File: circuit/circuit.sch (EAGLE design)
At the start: 60 parts, among them IC1 74HC04N, X1 PSS 254/8G

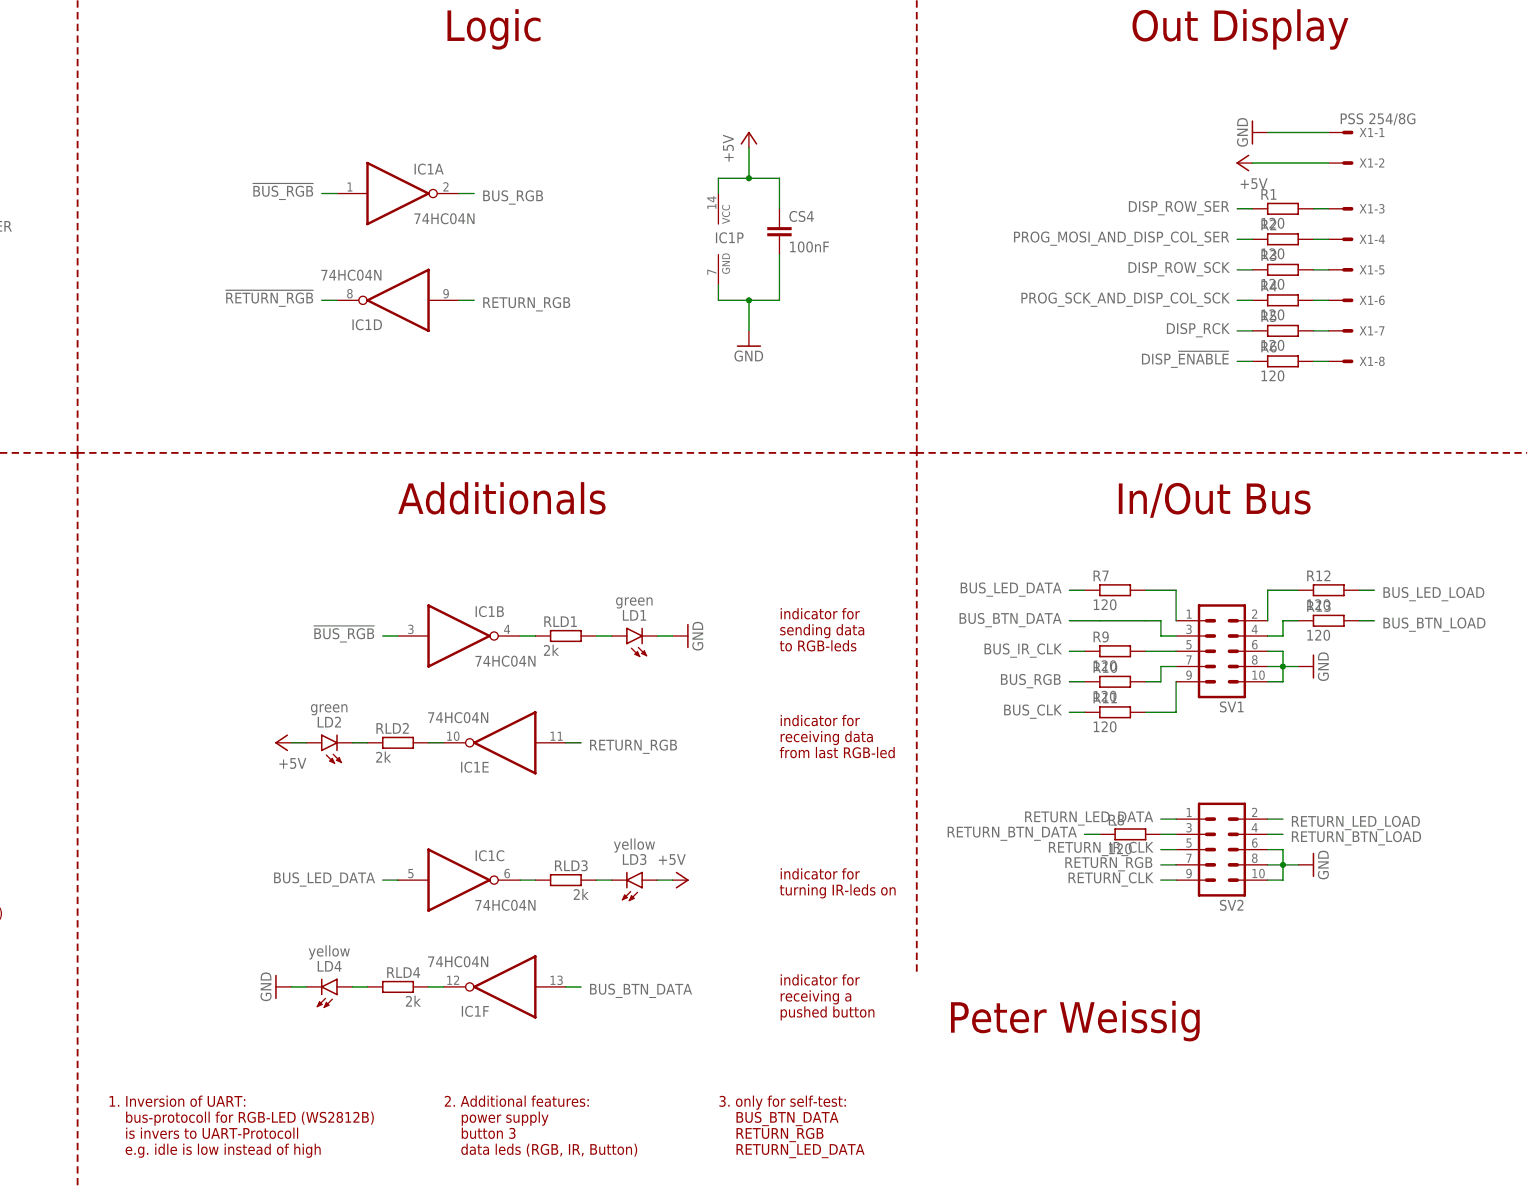
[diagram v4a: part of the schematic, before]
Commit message: updated circuit   + changed font type and size (e.g. fixed size of url)   + updated cooling pad for voltage regulator   + added more spacing at buttons (between pinheads and resistors)   + updated part-list
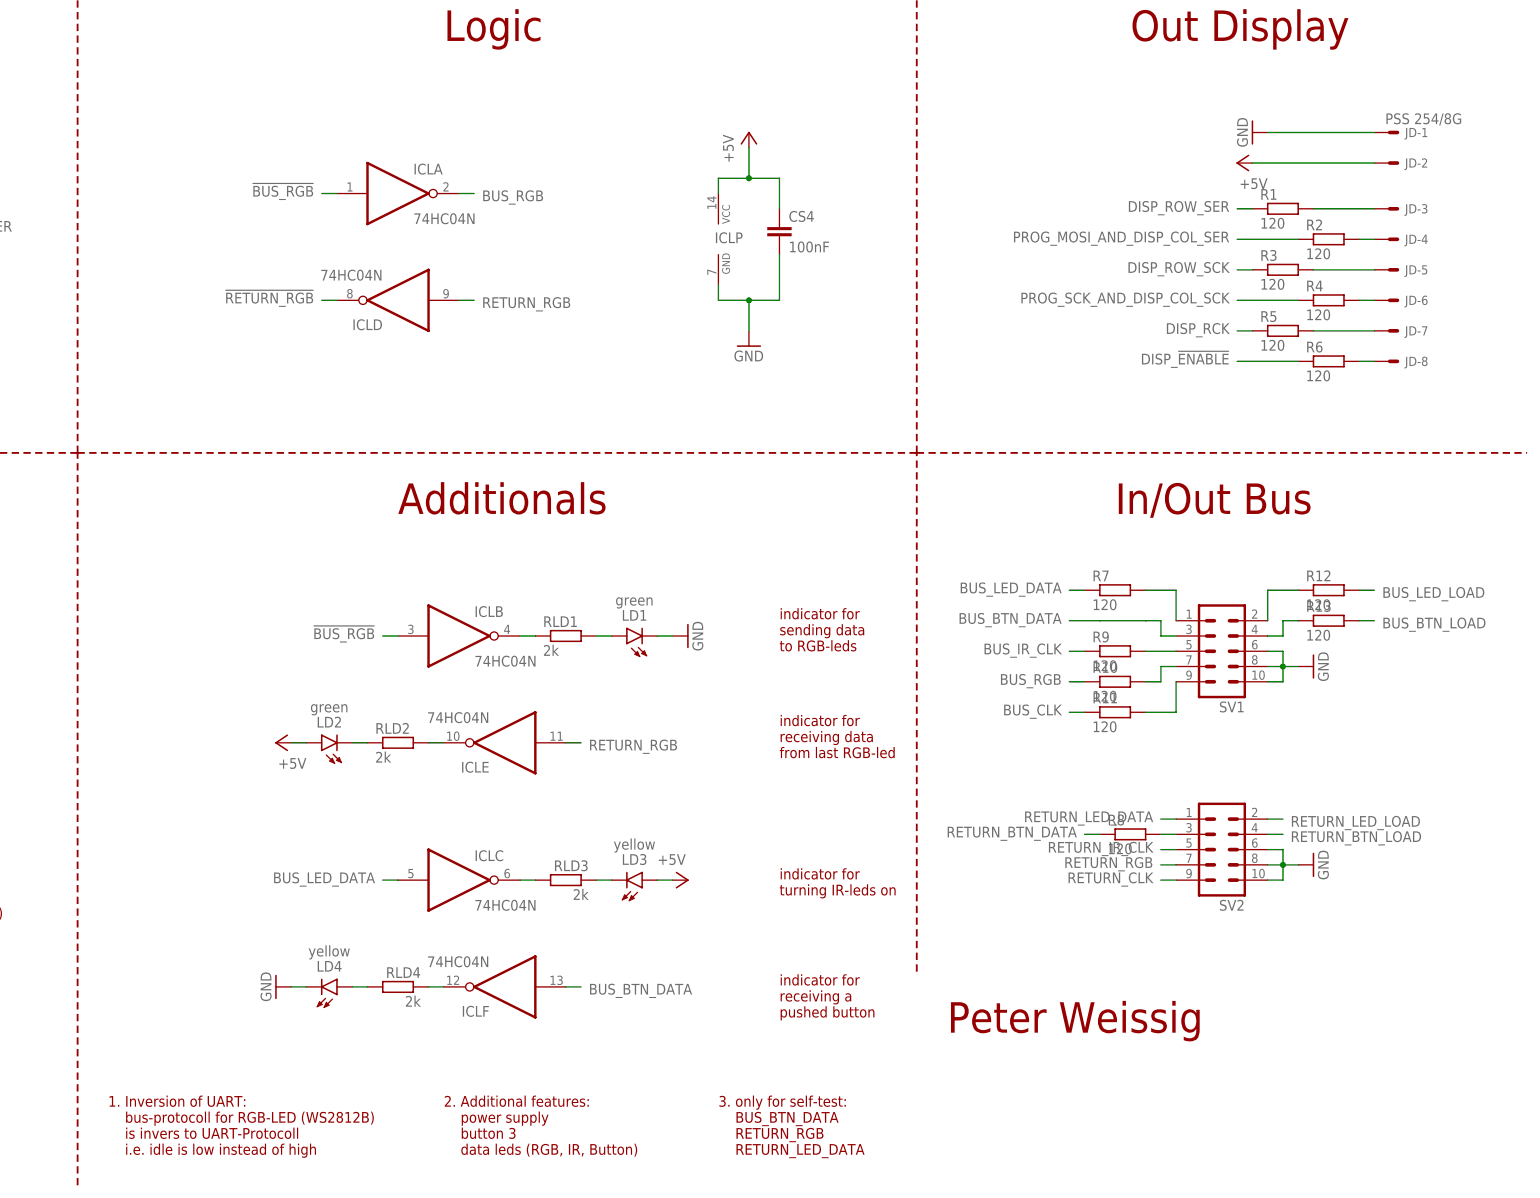
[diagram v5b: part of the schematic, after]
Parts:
- removed X1: PSS 254/8G, con-molex:22-23-2081
- added JD: PSS 254/8G, con-molex:22-23-2081
- renumbered IC1 to ICL
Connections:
- net +5V: now also JD-2.S; no longer X1-2.S
- net GND: now also JD-1.S; no longer X1-1.S
- net N$20: now also JD-3.S; no longer X1-3.S
- net N$21: now also JD-4.S; no longer X1-4.S
- net N$22: now also JD-5.S; no longer X1-5.S
- net N$23: now also JD-6.S; no longer X1-6.S
- net N$24: now also JD-7.S; no longer X1-7.S
- net N$25: now also JD-8.S; no longer X1-8.S
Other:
- note added: "1. Inversion of UART: bus-protocoll for RGB-LED (WS2812B) is invers to UART-Protocoll i.e. idle is low instead of high"
- note removed: "1. Inversion of UART: bus-protocoll for RGB-LED (WS2812B) is invers to UART-Protocoll e.g. idle is low instead of high"
- moved on the sheet: R2, R4, R6

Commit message: minor fixes:   + updated crystal from 16 to 20 MHz   + updated package for SMD resistors (1206 instead of 0805)   + fixed wrong caption (from 2019 to 2020) ==> newly exported images and elecrow files ==> updated part list and reichelt shopping cart
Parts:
- R1, R10, R11, R12, R13, R2, R3, R4, R5, R6, R7, R8, R9: device rcl:R-EU_R0805 -> rcl:R-EU_R1206W
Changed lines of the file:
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@@
 <grid distance="0.1" unitdist="inch" unit="inch" style="lines" multiple="1" display="no" altdistance="0.01" altunitdist="inch" altunit="inch"/>
 <layers>
-<layer number="1" name="Top" color="4" fill="1" visible="no" active="no"/>
-<layer number="16" name="Bottom" color="1" fill="1" visible="no" active="no"/>
-<layer number="17" name="Pads" color="2" fill="1" visible="no" active="no"/>
-<layer number="18" name="Vias" color="2" fill="1" visible="no" active="no"/>
-<layer number="19" name="Unrouted" color="6" fill="1" visible="no" active="no"/>
-<layer number="20" name="Dimension" color="15" fill="1" visible="no" active="no"/>
-<layer number="21" name="tPlace" color="7" fill="1" visible="no" active="no"/>
-<layer number="22" name="bPlace" color="7" fill="1" visible="no" active="no"/>
-<layer number="23" name="tOrigins" color="15" fill="1" visible="no" active="no"/>
-<layer number="24" name="bOrigins" color="15" fill="1" visible="no" active="no"/>
-<layer number="25" name="tNames" color="7" fill="1" visible="no" active="no"/>
-<layer number="26" name="bNames" color="7" fill="1" visible="no" active="no"/>
-<layer number="27" name="tValues" color="7" fill="1" visible="no" active="no"/>
-<layer number="28" name="bValues" color="7" fill="1" visible="no" active="no"/>
+<layer number="1" name="Top" color="4" fill="1" visible="yes" active="no"/>
+<layer number="16" name="Bottom" color="1" fill="1" visible="yes" active="no"/>
+<layer number="17" name="Pads" color="2" fill="1" visible="yes" active="no"/>
+<layer number="18" name="Vias" color="2" fill="1" visible="yes" active="no"/>
+<layer number="19" name="Unrouted" color="6" fill="1" visible="yes" active="no"/>
+<layer number="20" name="Dimension" color="15" fill="1" visible="yes" active="no"/>
+<layer number="21" name="tPlace" color="7" fill="1" visible="yes" active="no"/>
+<layer number="22" name="bPlace" color="7" fill="1" visible="yes" active="no"/>
+<layer number="23" name="tOrigins" color="15" fill="1" visible="yes" active="no"/>
+<layer number="24" name="bOrigins" color="15" fill="1" visible="yes" active="no"/>
+<layer number="25" name="tNames" color="7" fill="1" visible="yes" active="no"/>
+<layer number="26" name="bNames" color="7" fill="1" visible="yes" active="no"/>
+<layer number="27" name="tValues" color="7" fill="1" visible="yes" active="no"/>
+<layer number="28" name="bValues" color="7" fill="1" visible="yes" active="no"/>
 <layer number="29" name="tStop" color="7" fill="3" visible="no" active="no"/>
 <layer number="30" name="bStop" color="7" fill="6" visible="no" active="no"/>
@@
 <layer number="35" name="tGlue" color="7" fill="4" visible="no" active="no"/>
 <layer number="36" name="bGlue" color="7" fill="5" visible="no" active="no"/>
-<layer number="37" name="tTest" color="7" fill="1" visible="no" active="no"/>
-<layer number="38" name="bTest" color="7" fill="1" visible="no" active="no"/>
+<layer number="37" name="tTest" color="7" fill="1" visible="yes" active="no"/>
+<layer number="38" name="bTest" color="7" fill="1" visible="yes" active="no"/>
 <layer number="39" name="tKeepout" color="4" fill="11" visible="no" active="no"/>
 <layer number="40" name="bKeepout" color="1" fill="11" visible="no" active="no"/>
@@
 <layer number="44" name="Drills" color="7" fill="1" visible="no" active="no"/>
 <layer number="45" name="Holes" color="7" fill="1" visible="no" active="no"/>
-<layer number="46" name="Milling" color="3" fill="1" visible="no" active="no"/>
-<layer number="47" name="Measures" color="7" fill="1" visible="no" active="no"/>
-<layer number="48" name="Document" color="7" fill="1" visible="no" active="no"/>
-<layer number="49" name="Reference" color="7" fill="1" visible="no" active="no"/>
-<layer number="50" name="dxf" color="7" fill="1" visible="no" active="no"/>
-<layer number="51" name="tDocu" color="7" fill="1" visible="no" active="no"/>
-<layer number="52" name="bDocu" color="7" fill="1" visible="no" active="no"/>
-<layer number="53" name="tPadExt" color="7" fill="1" visible="no" active="no"/>
-<layer number="54" name="bPadExt" color="1" fill="1" visible="no" active="no"/>
-<layer number="56" name="wert" color="7" fill="1" visible="no" active="no"/>
+<layer number="46" name="Milling" color="3" fill="1" visible="yes" active="no"/>
+<layer number="47" name="Measures" color="7" fill="1" visible="yes" active="no"/>
+<layer number="48" name="Document" color="7" fill="1" visible="yes" active="no"/>
+<layer number="49" name="Reference" color="7" fill="1" visible="yes" active="no"/>
+<layer number="50" name="dxf" color="7" fill="1" visible="yes" active="no"/>
+<layer number="51" name="tDocu" color="7" fill="1" visible="yes" active="no"/>
+<layer number="52" name="bDocu" color="7" fill="1" visible="yes" active="no"/>
+<layer number="53" name="tPadExt" color="7" fill="1" visible="yes" active="no"/>
+<layer number="54" name="bPadExt" color="1" fill="1" visible="yes" active="no"/>
+<layer number="56" name="wert" color="7" fill="1" visible="yes" active="no"/>
 <layer number="91" name="Nets" color="2" fill="1" visible="yes" active="yes"/>
 <layer number="92" name="Busses" color="1" fill="1" visible="yes" active="yes"/>
@@
 <part name="LD4" library="robo_ag" deviceset="LED" device="-3MM" value="yellow"/>
 <part name="GND30" library="supply1" deviceset="GND" device=""/>
-<part name="R1" library="rcl" deviceset="R-EU_" device="R0805" value="120"/>
-<part name="R2" library="rcl" deviceset="R-EU_" device="R0805" value="120"/>
-<part name="R3" library="rcl" deviceset="R-EU_" device="R0805" value="120"/>
-<part name="R4" library="rcl" deviceset="R-EU_" device="R0805" value="120"/>
-<part name="R5" library="rcl" deviceset="R-EU_" device="R0805" value="120"/>
-<part name="R6" library="rcl" deviceset="R-EU_" device="R0805" value="120"/>
-<part name="R7" library="rcl" deviceset="R-EU_" device="R0805" value="120"/>
-<part name="R9" library="rcl" deviceset="R-EU_" device="R0805" value="120"/>
-<part name="R10" library="rcl" deviceset="R-EU_" device="R0805" value="120"/>
-<part name="R11" library="rcl" deviceset="R-EU_" device="R0805" value="120"/>
-<part name="R12" library="rcl" deviceset="R-EU_" device="R0805" value="120"/>
-<part name="R13" library="rcl" deviceset="R-EU_" device="R0805" value="120"/>
-<part name="R8" library="rcl" deviceset="R-EU_" device="R0805" value="120"/>
+<part name="R1" library="rcl" deviceset="R-EU_" device="R1206W" value="120"/>
+<part name="R2" library="rcl" deviceset="R-EU_" device="R1206W" value="120"/>
+<part name="R3" library="rcl" deviceset="R-EU_" device="R1206W" value="120"/>
+<part name="R4" library="rcl" deviceset="R-EU_" device="R1206W" value="120"/>
+<part name="R5" library="rcl" deviceset="R-EU_" device="R1206W" value="120"/>
+<part name="R6" library="rcl" deviceset="R-EU_" device="R1206W" value="120"/>
+<part name="R7" library="rcl" deviceset="R-EU_" device="R1206W" value="120"/>
+<part name="R9" library="rcl" deviceset="R-EU_" device="R1206W" value="120"/>
+<part name="R10" library="rcl" deviceset="R-EU_" device="R1206W" value="120"/>
+<part name="R11" library="rcl" deviceset="R-EU_" device="R1206W" value="120"/>
+<part name="R12" library="rcl" deviceset="R-EU_" device="R1206W" value="120"/>
+<part name="R13" library="rcl" deviceset="R-EU_" device="R1206W" value="120"/>
+<part name="R8" library="rcl" deviceset="R-EU_" device="R1206W" value="120"/>
 </parts>
 <sheets>
